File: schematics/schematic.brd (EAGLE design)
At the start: 180.3 x 63.5 mm, 22 parts, among them U1 TSR_1-2450

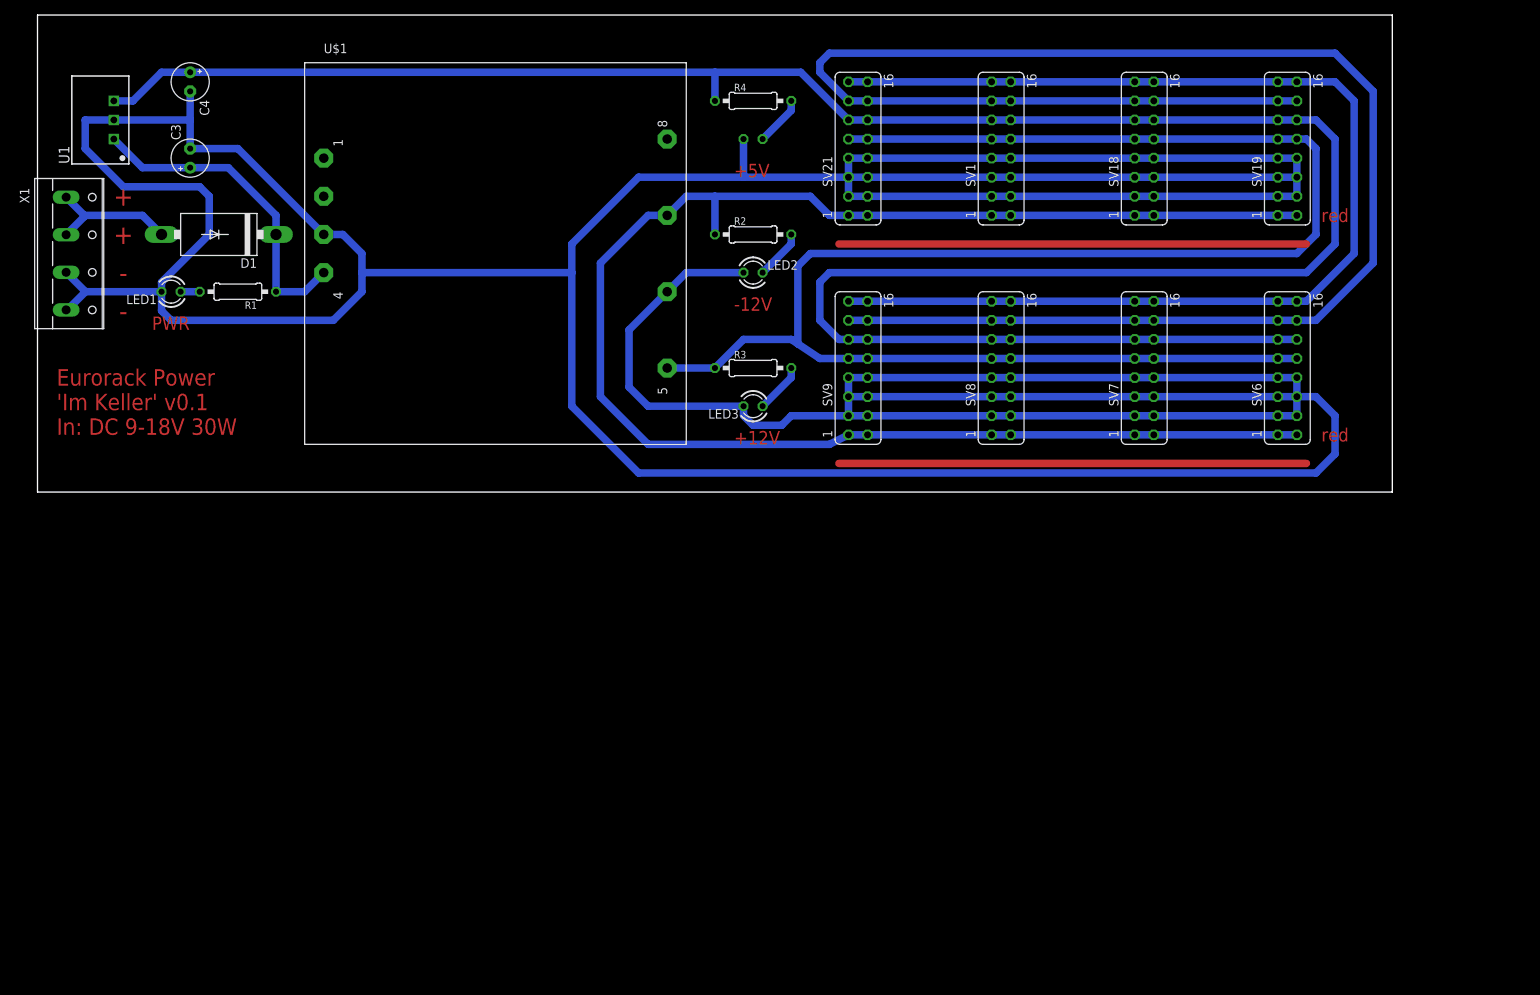
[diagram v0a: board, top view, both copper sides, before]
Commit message: replaced dc dc converter with smaller 15W version
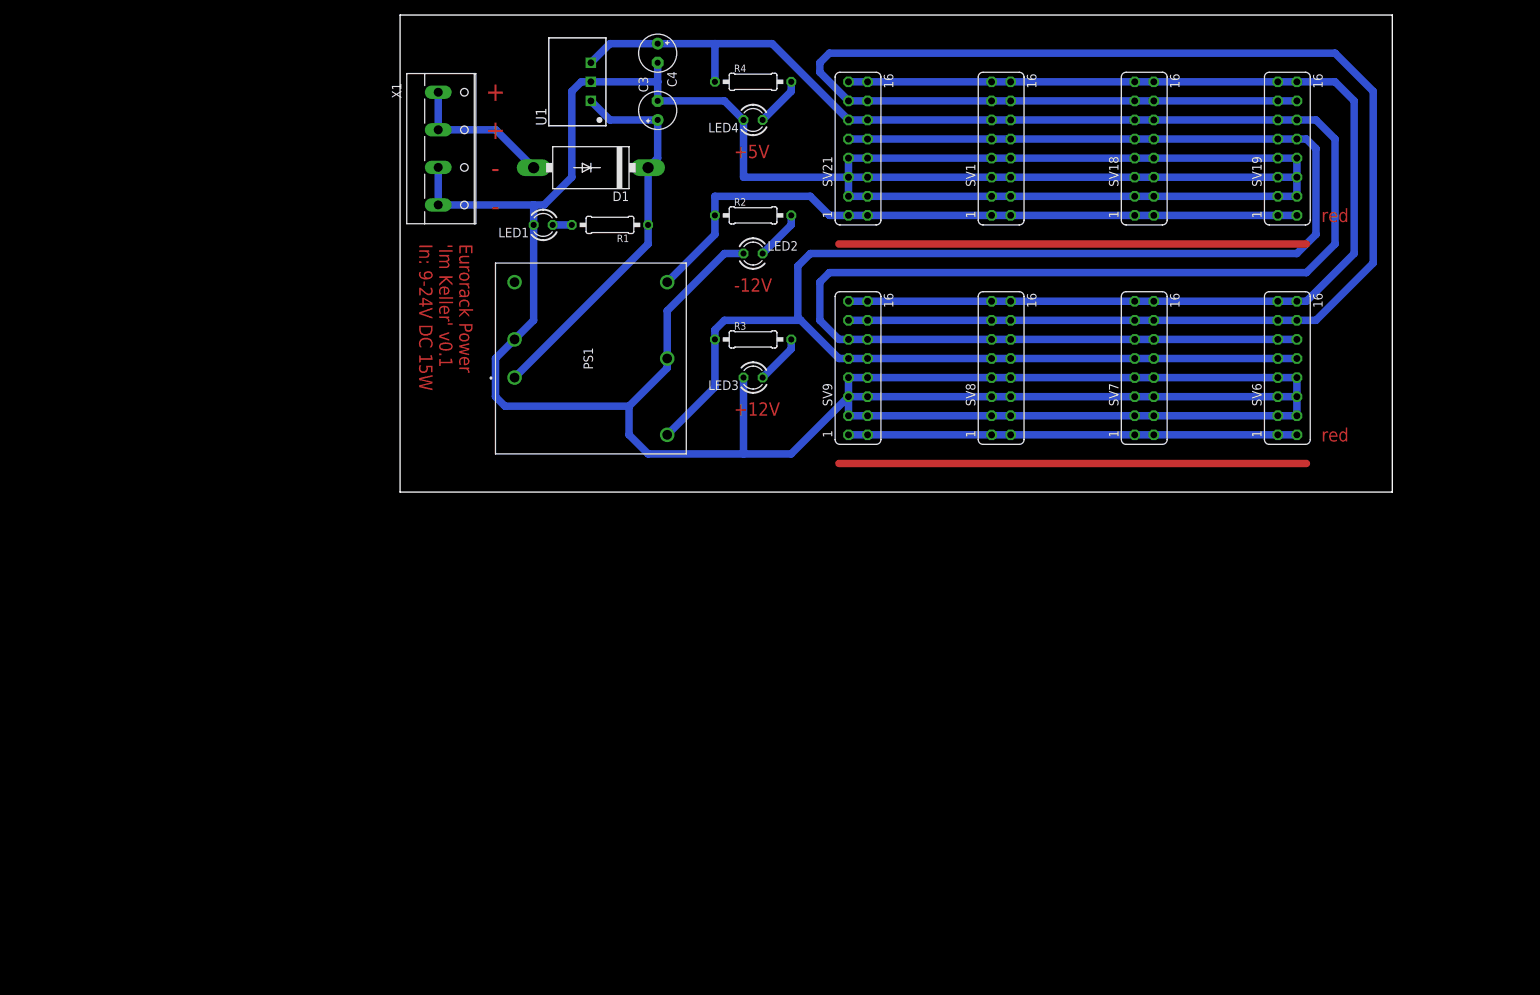
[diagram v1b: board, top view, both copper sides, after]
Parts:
- removed U$1: (no value), dk30a:DKA
- added PS1: DKMW30F-15, DKMW30F-15:DKMW30F15
- R1: value 820 Ohm -> 1200 Ohm
- moved U1 63.7 mm to (73.7, 54.6)
- moved C3 62.6 mm to (82.5, 50.8)
- moved C4 62.3 mm to (82.5, 58.4)
- moved X1 51.5 mm to (54.6, 45.7)
- moved D1 50.3 mm to (73.7, 43.2)
- moved LED1 50.3 mm to (67.3, 35.6)
- moved R1 50.3 mm to (76.2, 35.6)
- moved LED3 3.81 mm to (95.2, 15.2)
- moved R3 3.81 mm to (95.2, 20.3)
- moved LED2 2.54 mm to (95.2, 31.8)
- moved LED4 2.54 mm to (95.2, 49.5), flipped to the top, turned to 180 degrees
- moved R2 2.54 mm to (95.2, 36.8)
- moved R4 2.54 mm to (95.2, 54.6)
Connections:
- net +12V: now also PS1.3; no longer U$1.5
- net -12V: now also PS1.5; no longer U$1.7
- net GND: now also PS1.2, PS1.4; no longer U$1.3, U$1.6
- net VI: now also PS1.1; no longer U$1.4
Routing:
- net GND: track 792.0 -> 586.9 mm
- net -12V: track 215.9 -> 152.3 mm
- net +5V: track 325.9 -> 264.7 mm
- net VI: track 43.4 -> 52.1 mm
- net +12V: track 241.4 -> 249.0 mm
- net +15V: track 18.4 -> 19.8 mm
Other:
- board size 180.3 x 63.5 mm -> 132.1 x 63.5 mm
- board text added: "Eurorack Power 'Im Keller' v0.1 In: 9-24V DC 15W"
- board text removed: "Eurorack Power 'Im Keller' v0.1 In: DC 9-18V 30W"
- board text removed: "PWR"

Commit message: removed airwires, added dkmw30f lib
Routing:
- net GND: track 586.9 -> 734.3 mm
- net -12V: track 152.3 -> 225.0 mm
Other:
- board text added: "Eurorack Power 'Im Keller' v0.1 In: 12-24V DC 15W"
- board text removed: "Eurorack Power 'Im Keller' v0.1 In: 9-24V DC 15W"
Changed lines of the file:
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@@
 <text x="50.8" y="33.02" size="1.778" layer="1" font="fixed" rot="SR270">Eurorack Power
 'Im Keller' v0.1
-In: 9-24V DC 15W</text>
+In: 12-24V DC 15W</text>
 <text x="92.71" y="44.45" size="1.778" layer="1">+5V</text>
 <text x="92.71" y="26.67" size="1.778" layer="1">-12V</text>
@@
 <wire x1="60.96" y1="17.78" x2="60.96" y2="12.7" width="1" layer="16"/>
 <wire x1="60.96" y1="12.7" x2="62.23" y2="11.43" width="1" layer="16"/>
-<wire x1="62.23" y1="11.43" x2="78.74" y2="11.43" width="1" layer="16"/>
+<wire x1="62.23" y1="11.43" x2="72.39" y2="11.43" width="1" layer="16"/>
+<wire x1="72.39" y1="11.43" x2="78.74" y2="11.43" width="1" layer="16"/>
 <wire x1="78.74" y1="11.43" x2="83.82" y2="16.51" width="1" layer="16"/>
 <wire x1="83.82" y1="16.51" x2="83.82" y2="17.78" width="1" layer="16"/>
-<wire x1="78.74" y1="11.43" x2="78.74" y2="7.62" width="1" layer="16"/>
-<wire x1="78.74" y1="7.62" x2="81.28" y2="5.08" width="1" layer="16"/>
-<wire x1="81.28" y1="5.08" x2="93.98" y2="5.08" width="1" layer="16"/>
-<wire x1="93.98" y1="15.24" x2="93.98" y2="5.08" width="1" layer="16"/>
 <wire x1="93.98" y1="31.75" x2="91.44" y2="31.75" width="1" layer="16"/>
 <wire x1="91.44" y1="31.75" x2="83.82" y2="24.13" width="1" layer="16"/>
@@
 <wire x1="82.55" y1="54.61" x2="82.55" y2="52.07" width="1" layer="16"/>
 <wire x1="82.55" y1="52.07" x2="91.44" y2="52.07" width="1" layer="16"/>
-<wire x1="53.34" y1="43.22" x2="53.34" y2="38.1" width="1" layer="16"/>
-<wire x1="53.34" y1="38.22" x2="66.04" y2="38.22" width="1" layer="16"/>
-<wire x1="66.04" y1="38.22" x2="67.43" y2="38.22" width="1" layer="16"/>
+<wire x1="67.43" y1="38.22" x2="66.04" y2="38.22" width="1" layer="16"/>
 <wire x1="67.43" y1="38.22" x2="71.12" y2="41.91" width="1" layer="16"/>
 <wire x1="66.04" y1="38.22" x2="66.04" y2="35.56" width="1" layer="16"/>
@@
 <wire x1="91.44" y1="52.07" x2="93.98" y2="49.53" width="1" layer="16"/>
 <wire x1="93.98" y1="49.53" x2="93.98" y2="41.91" width="1" layer="16"/>
-<wire x1="93.98" y1="5.08" x2="100.33" y2="5.08" width="1" layer="16"/>
-<wire x1="100.33" y1="5.08" x2="107.95" y2="12.7" width="1" layer="16"/>
-<wire x1="53.34" y1="38.22" x2="53.34" y2="38.1" width="0" layer="19" extent="16-16"/>
+<wire x1="167.64" y1="12.7" x2="170.18" y2="12.7" width="1" layer="16"/>
+<wire x1="170.18" y1="12.7" x2="171.45" y2="11.43" width="1" layer="16"/>
+<wire x1="171.45" y1="11.43" x2="171.45" y2="3.81" width="1" layer="16"/>
+<wire x1="171.45" y1="3.81" x2="170.18" y2="2.54" width="1" layer="16"/>
+<wire x1="76.2" y1="2.54" x2="72.39" y2="6.35" width="1" layer="16"/>
+<wire x1="72.39" y1="6.35" x2="72.39" y2="11.43" width="1" layer="16"/>
+<wire x1="170.18" y1="2.54" x2="76.2" y2="2.54" width="1" layer="16"/>
+<wire x1="93.98" y1="15.24" x2="93.98" y2="13.97" width="1" layer="16"/>
+<wire x1="93.98" y1="13.97" x2="95.25" y2="12.7" width="1" layer="16"/>
+<wire x1="95.25" y1="12.7" x2="107.95" y2="12.7" width="1" layer="16"/>
+<wire x1="66.04" y1="38.22" x2="53.34" y2="38.22" width="1" layer="16"/>
+<wire x1="53.34" y1="38.22" x2="53.34" y2="43.22" width="1" layer="16"/>
+<wire x1="127" y1="44.45" x2="127" y2="39.37" width="1" layer="16"/>
+<wire x1="146.05" y1="44.45" x2="146.05" y2="39.37" width="1" layer="16"/>
+<wire x1="146.05" y1="15.24" x2="146.05" y2="10.16" width="1" layer="16"/>
+<wire x1="127" y1="15.24" x2="127" y2="10.16" width="1" layer="16"/>
+<wire x1="110.49" y1="15.24" x2="110.49" y2="10.16" width="1" layer="16"/>
+<wire x1="129.54" y1="15.24" x2="129.54" y2="10.16" width="1" layer="16"/>
+<wire x1="148.59" y1="15.24" x2="148.59" y2="10.16" width="1" layer="16"/>
+<wire x1="165.1" y1="15.24" x2="165.1" y2="10.16" width="1" layer="16"/>
+<wire x1="165.1" y1="44.45" x2="165.1" y2="39.37" width="1" layer="16"/>
+<wire x1="148.59" y1="44.45" x2="148.59" y2="39.37" width="1" layer="16"/>
+<wire x1="129.54" y1="44.45" x2="129.54" y2="39.37" width="1" layer="16"/>
+<wire x1="110.49" y1="44.45" x2="110.49" y2="39.37" width="1" layer="16"/>
 </signal>
 <signal name="+15V">
@@
 <wire x1="83.82" y1="27.94" x2="90.17" y2="34.29" width="1" layer="16"/>
 <wire x1="90.17" y1="34.29" x2="90.17" y2="36.83" width="1" layer="16"/>
-<wire x1="167.64" y1="36.83" x2="167.64" y2="7.62" width="0" layer="19" extent="1-1"/>
+<wire x1="80.01" y1="8.89" x2="80.01" y2="6.35" width="1" layer="16"/>
+<wire x1="87.63" y1="16.51" x2="87.63" y2="22.86" width="1" layer="16"/>
+<wire x1="87.63" y1="22.86" x2="91.44" y2="26.67" width="1" layer="16"/>
+<wire x1="91.44" y1="26.67" x2="95.25" y2="26.67" width="1" layer="16"/>
+<wire x1="95.25" y1="26.67" x2="105.41" y2="36.83" width="1" layer="16"/>
+<wire x1="80.01" y1="8.89" x2="87.63" y2="16.51" width="1" layer="16"/>
+<wire x1="80.01" y1="6.35" x2="81.28" y2="5.08" width="1" layer="16"/>
+<wire x1="105.41" y1="5.08" x2="107.95" y2="7.62" width="1" layer="16"/>
+<wire x1="81.28" y1="5.08" x2="105.41" y2="5.08" width="1" layer="16"/>
 </signal>
 <signal name="+5V">
@@
 </signal>
 <signal name="N$1">
-<wire x1="106.68" y1="3.81" x2="168.91" y2="3.81" width="1" layer="1"/>
+<wire x1="106.68" y1="5.08" x2="168.91" y2="5.08" width="1" layer="1"/>
 </signal>
 <signal name="N$6">
-<wire x1="106.68" y1="33.02" x2="168.91" y2="33.02" width="1" layer="1"/>
+<wire x1="106.68" y1="34.29" x2="168.91" y2="34.29" width="1" layer="1"/>
 </signal>
 </signals>

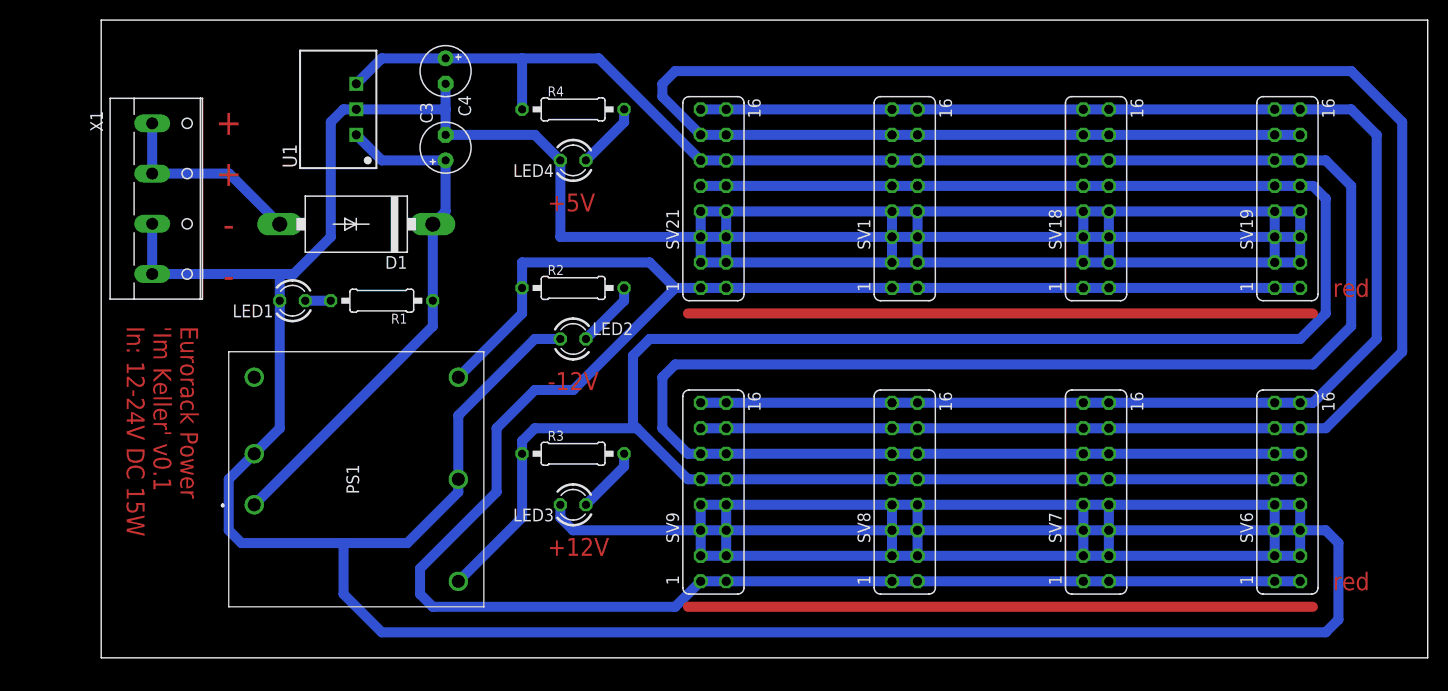
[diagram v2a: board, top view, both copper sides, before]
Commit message: added 2 crc groups
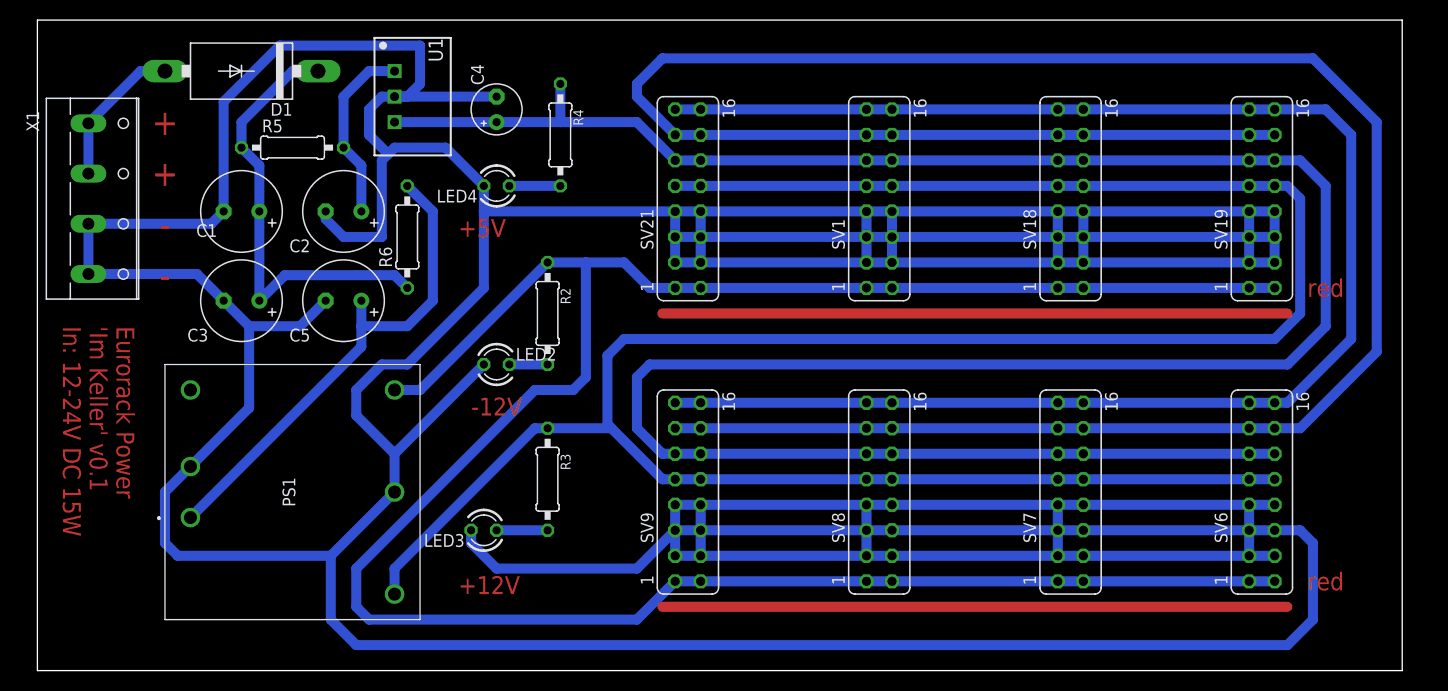
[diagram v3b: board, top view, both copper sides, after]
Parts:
- removed LED1: (no value), led:LED3MM
- removed R1: 1200 Ohm, rcl:0207/10
- added C1, C2, C5: 100uF, rcl:E3,5-8
- added R5, R6: 1 Ohm, rcl:0207/10
- C3: value 22uF -> 100uF; device rcl:E2,5-5 -> rcl:E3,5-8
- moved C3 25.4 mm to (62.2, 35.6), turned to 180 degrees
- moved D1 19.1 mm to (62.2, 58.4)
- moved LED3 9.25 mm to (86.4, 12.7)
- moved LED2 8.03 mm to (87.6, 29.2)
- moved LED4 8.03 mm to (87.6, 47.0)
- moved PS1 6.48 mm to (57.1, 14.0)
- moved X1 6.35 mm to (48.3, 45.7)
- moved C4 6.35 mm to (87.6, 54.6), turned to 90 degrees
- moved U1 4.02 mm to (77.5, 55.9), turned to 270 degrees
- moved R2 3.59 mm to (92.7, 34.3), turned to 270 degrees
- moved R3 3.59 mm to (92.7, 17.8), turned to 270 degrees
- moved R4 2.84 mm to (94.0, 52.1), turned to 270 degrees
- moved SV1 2.54 mm to (125.7, 45.7)
- moved SV8 2.54 mm to (125.7, 16.5)
- moved SV18 2.54 mm to (144.8, 45.7)
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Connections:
- removed net N$2: LED1.A, R1.2
- new net N$8: C1.+, C3.+, D1.C, R5.1, R6.1
- new net VI1: C5.+, PS1.1, R6.2
- net GND: now also C1.-, C2.-, C5.-; no longer LED1.K
- net VI: now also C2.+, R5.2; no longer C3.+, D1.C, PS1.1, R1.1
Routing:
- net GND: track 734.3 -> 819.0 mm
- net VI1: track 0.00 -> 49.3 mm
- net N$8: track 0.00 -> 44.6 mm
- net VI: track 52.1 -> 18.3 mm
- net +5V: track 264.7 -> 253.4 mm
- net -12V: track 225.0 -> 233.5 mm
- net +15V: track 19.8 -> 14.8 mm
- net N$3: track 6.66 -> 3.81 mm
- net N$2: track 2.54 -> 0.00 mm
- net N$4: track 6.66 -> 5.08 mm
- net N$5: track 6.66 -> 5.08 mm
- net +12V: track 249.0 -> 250.3 mm
- net CV: track 238.5 -> 239.6 mm
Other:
- board size 132.1 x 63.5 mm -> 135.9 x 64.8 mm

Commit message: bugfixes
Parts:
- moved R4 1.27 mm to (92.7, 52.1)
- moved SV1 1.27 mm to (124.5, 45.7)
- moved SV18 1.27 mm to (143.5, 45.7)
- moved SV19 1.27 mm to (162.6, 45.7)
- moved SV21 1.27 mm to (105.4, 45.7)
- moved SV6 1.27 mm to (162.6, 16.5)
- moved SV7 1.27 mm to (143.5, 16.5)
- moved SV8 1.27 mm to (124.5, 16.5)
- moved SV9 1.27 mm to (105.4, 16.5)
- moved LED3 1.27 mm to (87.6, 12.7)
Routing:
- net GND: track 819.0 -> 829.9 mm
- net -12V: track 233.5 -> 229.7 mm
- net +5V: track 253.4 -> 252.2 mm
- net N$5: track 5.08 -> 3.81 mm
- net N$4: track 5.08 -> 3.81 mm
- net +12V: track 250.3 -> 249.1 mm
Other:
- board size 135.9 x 64.8 mm -> 134.6 x 64.8 mm
